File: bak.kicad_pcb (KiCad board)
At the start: 2 copper layers, 50 x 52 mm, 67 parts, among them CON1 IR_RECIEVER, CON2 HALL_SENSOR1, CON3 HALL_SENSOR2, CON4 Conn_01x03, CON5 Conn_01x03, IC1 A3G4250DTR, IC2 MCP112T-195I_TT, IC3 RN4871-V_RM140, IC4 MC3479, J1 USB_B_Micro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

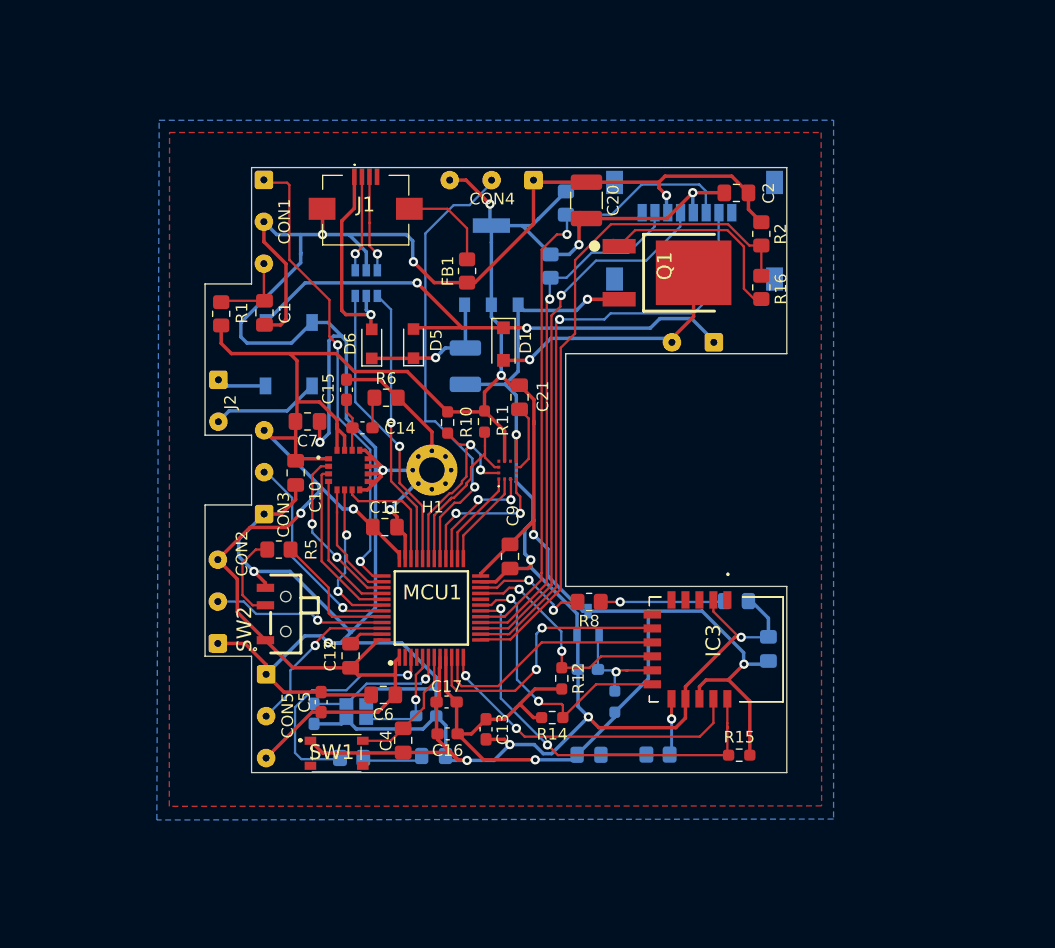
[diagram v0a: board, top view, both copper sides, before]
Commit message: update predelane piny a spi
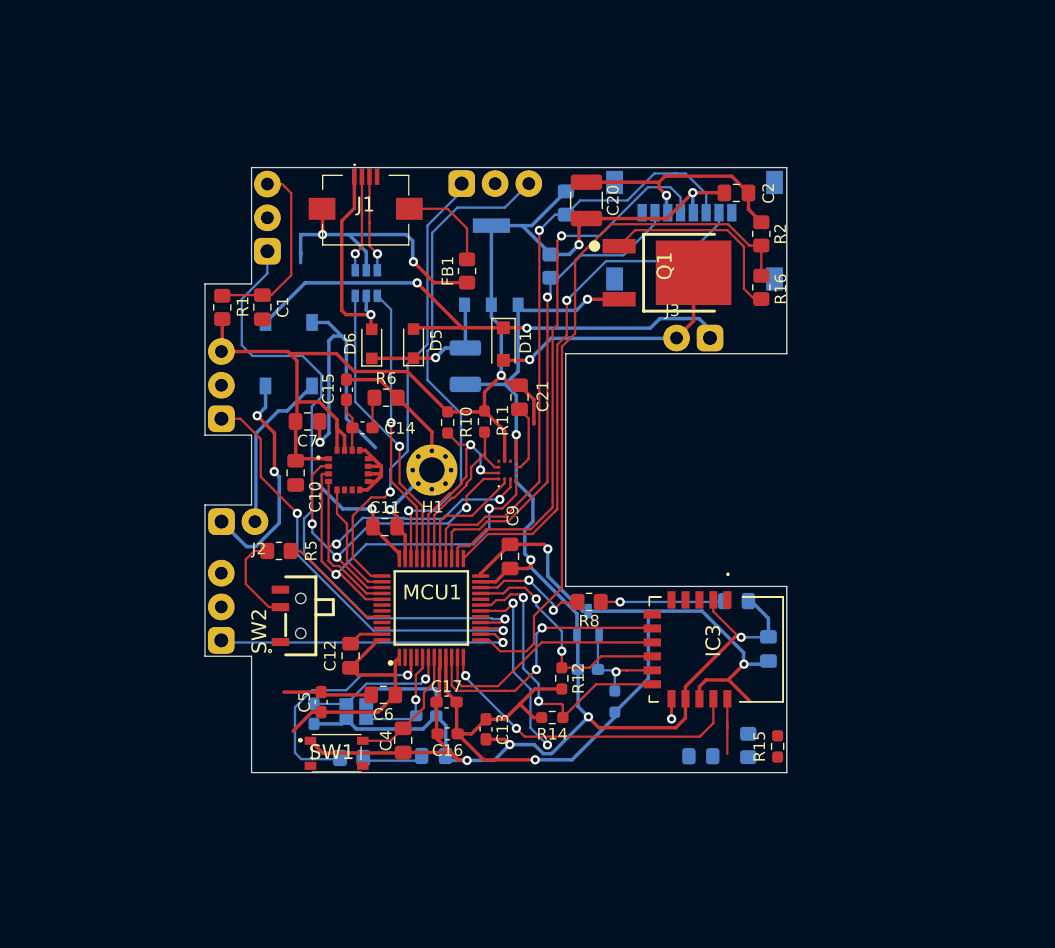
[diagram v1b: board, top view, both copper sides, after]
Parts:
- removed CON5: Conn_01x03, Connector_Wire:SolderWire-0.1sqmm_1x03_P3.6mm_D0.4mm_OD1mm
- CON1, CON2, CON3: footprint Connector_Wire:SolderWire-0.1sqmm_1x03_P3.6mm_D0.4mm_OD1mm -> KICAD_bak:MyConnector3
- CON4: value Conn_01x03 -> SWD; footprint Connector_Wire:SolderWire-0.1sqmm_1x03_P3.6mm_D0.4mm_OD1mm -> KICAD_bak:MyConnector3
- D2: value D_Bridge_+A-A -> Usměrňovací můstek ABS210-13
- IC4: value MC3479 -> Akcelerometr MC3479
- J2: footprint Connector_Wire:SolderWire-0.1sqmm_1x02_P3.6mm_D0.4mm_OD1mm -> KICAD_bak:MyConnector2
- J3: footprint Connector_Wire:SolderWire-0.1sqmm_1x02_P3.6mm_D0.4mm_OD1mm -> KICAD_bak:MyConnector2; moved to F.Cu
- moved CON3 11.7 mm to (50.1, 51.2)
- moved J2 10.3 mm to (53.0, 60.5), turned to 0 degrees
- moved D7 9.61 mm to (91.3, 83.1)
- moved R13 7.80 mm to (95.4, 82.2), turned to 270 degrees
- moved J3 3.83 mm to (89.2, 49.6)
- moved R15 3.38 mm to (97.9, 82.2), turned to 90 degrees
- moved CON4 3.31 mm to (73.7, 33.9), turned to 0 degrees
- moved CON1 3.27 mm to (54.1, 36.8), turned to 90 degrees
- moved CON2 3.15 mm to (50.1, 70.2)
- moved SW2 1.30 mm to (55.2, 70.3)
- moved R1 0.56 mm to (50.2, 44.5)
- moved C1 0.52 mm to (53.7, 44.5)
- moved R5 0.12 mm to (55.1, 65.4)
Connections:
- net /SPI3_CS renamed /SPI3_CS1
- CON2 pad 1: GND -> /HALL1
- CON2 pad 2: /HALL1 -> GND
- CON3 pad 1: GND -> /HALL2
- CON3 pad 2: /HALL2 -> GND
- CON4 pad 1: GND -> /SWCLK
- CON4 pad 2: /CON1 -> GND
- CON4 pad 3: +3.3VA -> /SWDIO
- IC4 pad 1: /SPI2_SCK -> /SPI3_SCK
- IC4 pad 2: /SPI2_CS -> /SPI3_CS2
- IC4 pad 3: /SPI2_MISO -> /SPI3_MISO
- IC4 pad 4: /SPI2_MOSI -> /SPI3_MOSI
- J4 pad 2: /SPI1_CS -> /SPI2_CS
- J4 pad 3: /SPI1_MOSI -> /SPI2_MOSI
- J4 pad 5: /SPI1_SCK -> /SPI2_SCK
- J4 pad 7: /SPI1_MISO -> /SPI2_MISO
- MCU1 pad 14: /SPI1_CS -> /HALL1
- MCU1 pad 15: /SPI1_SCK -> /HALL2
- MCU1 pad 16: /SPI1_MISO -> /IR_OUT
- MCU1 pad 17: /SPI1_MOSI -> Net-(MCU1-Pad17)
- MCU1 pad 29: /CON1 -> /SPI3_CS2
- MCU1 pad 34: /GYRO_INT -> /SWDIO
- MCU1 pad 37: /IR_OUT -> /SWCLK
- MCU1 pad 42: /GYRO_DRDY -> /I2C_SCL
- MCU1 pad 43: /HALL2 -> Net-(MCU1-Pad43)
- MCU1 pad 45: /HALL1 -> Net-(MCU1-Pad45)
- MCU1 pad 46: /CON2 -> /I2C_SDA
- R3 pad 1: /SPI1_MOSI -> /SPI2_MOSI
- R4 pad 1: /SPI1_MISO -> /SPI2_MISO
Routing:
- net GND: track 391.2 -> 271.9 mm, vias 15 -> 12
- net +3.3VA: track 293.0 -> 231.8 mm, vias 9 -> 7
- net /SPI1_MOSI: track 55.0 -> 0.00 mm, vias 1 -> 0
- net /SPI1_CS: track 52.4 -> 0.00 mm, vias 1 -> 0
- net /SPI1_SCK: track 46.5 -> 0.00 mm, vias 1 -> 0
- net /SPI1_MISO: track 45.2 -> 0.00 mm, vias 1 -> 0
- net /SWDIO: track 0.00 -> 42.8 mm, vias 0 -> 1
- net /SPI2_MOSI: track 12.8 -> 52.9 mm, vias 2 -> 1
- net /SWCLK: track 0.00 -> 39.9 mm, vias 0 -> 1
- net /SPI2_SCK: track 8.32 -> 47.8 mm, vias 0 -> 1
- net /CON1: track 39.2 -> 0.00 mm, vias 1 -> 0
- net /SPI2_CS: track 8.32 -> 45.0 mm, vias 0 -> 1
- net /SPI2_MISO: track 10.7 -> 42.0 mm, vias 2 -> 1
- net /HALL2: track 18.1 -> 39.3 mm, vias 1 -> 2
- net /SPI3_MOSI: track 14.6 -> 35.3 mm, vias 0 -> 2
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- removed copper zone on F.Cu, net (none)
- removed copper zone on B.Cu, net GND

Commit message: pred ble modulem uprava
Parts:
- added C23: 100n, Capacitor_SMD:C_0805_2012Metric_Pad1.18x1.45mm_HandSolder, F.Cu at (54.6, 76.4)
- added SW3: SW_Push_Open, SamacSys_Parts:PTS815SJM250SMTRLFS, F.Cu at (54.5, 81.0)
- U1: moved to F.Cu
- moved FB1 13.5 mm to (57.8, 41.9)
- moved U1 0.98 mm to (61.6, 42.5)
- moved SW1 0.70 mm to (60.7, 82.7)
- moved J1 0.66 mm to (62.4, 35.5), turned to 180 degrees
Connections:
- MCU1 pad 45: Net-(MCU1-Pad45) -> /BTN
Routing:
- net GND: track 271.9 -> 234.8 mm, vias 12 -> 10
- net /BTN: track 0.00 -> 16.1 mm
- net +3.3VA: track 231.8 -> 221.7 mm
- net Net-(FB1-Pad2): track 8.32 -> 0.00 mm
- net /USB_CON-: track 8.53 -> 3.13 mm, vias 1 -> 0
- net +5V: track 17.8 -> 12.7 mm, vias 1 -> 0
- net /USB_CON+: track 8.52 -> 3.65 mm, vias 1 -> 0
- net /USB+: track 24.0 -> 25.1 mm, vias 1 -> 2
- net /NRST: track 11.1 -> 10.4 mm
- net /USB-: track 25.0 -> 25.4 mm, vias 1 -> 2

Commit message: cca predelano
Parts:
- D4, D7, R13: moved to F.Cu
- R12, R15: moved to B.Cu
- moved SW3 35.0 mm to (87.8, 70.2), turned to 180 degrees
- moved C23 28.6 mm to (82.5, 70.3), turned to 90 degrees
- moved R15 14.0 mm to (84.0, 83.7), turned to 180 degrees
- moved R13 14.0 mm to (82.4, 77.2), turned to 180 degrees
- moved R12 13.5 mm to (92.3, 72.8), turned to 0 degrees
- moved R8 12.4 mm to (94.1, 69.4)
- moved D7 9.48 mm to (82.5, 79.8), turned to 0 degrees
- moved IC3 8.68 mm to (93.0, 82.6), turned to 180 degrees
- moved IC2 5.50 mm to (86.9, 73.2)
- moved D4 3.43 mm to (97.8, 70.3), turned to 90 degrees
- moved C19 2.82 mm to (81.0, 78.4), turned to 270 degrees
- moved R5 1.50 mm to (53.6, 65.5)
- moved R14 1.49 mm to (79.0, 78.3), turned to 270 degrees
- moved C22 1.06 mm to (96.2, 73.3)
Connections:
- MCU1 pad 17: Net-(MCU1-Pad17) -> /BTN
- MCU1 pad 45: /BTN -> Net-(MCU1-Pad45)
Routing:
- net GND: track 234.8 -> 302.5 mm, vias 10 -> 15
- net +3.3VA: track 221.7 -> 272.2 mm, vias 7 -> 11
- net /DIODE2: track 10.3 -> 24.0 mm
- net /UART_RX: track 20.7 -> 30.2 mm
- net /UART_TX: track 23.9 -> 32.8 mm
- net Net-(D4-Pad2): track 10.7 -> 2.71 mm, vias 1 -> 0
- net /MODE: track 21.4 -> 28.0 mm
- net /UART_RTS: track 20.4 -> 26.1 mm
- net Net-(FB1-Pad2): track 0.00 -> 5.62 mm
- net /UART_TX_IND: track 27.8 -> 22.3 mm, vias 2 -> 4
- net /RST: track 9.17 -> 14.0 mm
- net /P0_2: track 1.73 -> 6.04 mm, vias 1 -> 0
- net Net-(D7-Pad1): track 0.00 -> 2.62 mm
- net /BTN: track 16.1 -> 13.8 mm, vias 0 -> 2
- net /UART_CTS: track 25.8 -> 27.7 mm
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- added copper zone on B.Cu, net GND
- added copper zone on F.Cu, net GND

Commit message: hotovo_snad
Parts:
- C2, C20, Q1, R16, R2: moved to B.Cu
- J4: moved to F.Cu
- moved R16 12.2 mm to (85.0, 46.8), turned to 180 degrees
- moved R2 10.5 mm to (91.2, 47.3), turned to 180 degrees
- moved C20 10.2 mm to (91.7, 35.1), turned to 180 degrees
- moved J3 7.85 mm to (94.9, 44.1), turned to 90 degrees
- moved J4 4.16 mm to (86.7, 39.4), turned to 180 degrees
- moved C2 2.72 mm to (97.1, 34.6), turned to 90 degrees
- moved FB1 2.43 mm to (57.7, 44.3)
- moved Q1 1.36 mm to (91.8, 40.8), turned to 90 degrees
- moved D3 0.99 mm to (67.8, 82.2)
- moved R7 0.89 mm to (61.2, 82.3)
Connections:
- net /I2C_SDA renamed Net-(MCU1-Pad46)
- MCU1 pad 38: /SPI3_CS1 -> /GYRO_INT
- MCU1 pad 42: /I2C_SCL -> /GYRO_DRDY
- MCU1 pad 43: Net-(MCU1-Pad43) -> /SPI3_CS1
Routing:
- net GND: track 302.5 -> 342.4 mm, vias 15 -> 17
- net +3.3VA: track 272.2 -> 306.3 mm, vias 11 -> 13
- net /GYRO_DRDY: track 0.00 -> 16.4 mm, vias 0 -> 2
- net /MOTOR_PWM: track 61.6 -> 46.4 mm, vias 0 -> 1
- net Net-(Q1-Pad1): track 19.1 -> 4.57 mm
- net /MOTOR-: track 21.3 -> 33.9 mm, vias 1 -> 3
- net /GYRO_INT: track 0.00 -> 9.66 mm
- net /SPI2_MOSI: track 52.9 -> 44.5 mm, vias 1 -> 2
- net /SPI2_CS: track 43.7 -> 36.3 mm, vias 1 -> 0
- net /SPI3_CS1: track 10.2 -> 16.6 mm, vias 0 -> 2
- net /MOTOR+: track 47.8 -> 51.7 mm, vias 2 -> 3
- net /SPI2_MISO: track 42.0 -> 46.0 mm, vias 1 -> 2
- net Net-(FB1-Pad2): track 5.62 -> 8.10 mm
- net /IR_OUT: track 55.2 -> 56.9 mm
- net /SPI2_SCK: track 47.0 -> 45.5 mm, vias 1 -> 0
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- removed copper zone on B.Cu, net GND
- removed copper zone on F.Cu, net GND

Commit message: snad final, zony, upraveny 3D modely, upraveny tlacitko
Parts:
- removed C23: 100n, Capacitor_SMD:C_0805_2012Metric_Pad1.18x1.45mm_HandSolder
- added R17: 10k, Resistor_SMD:R_0805_2012Metric_Pad1.20x1.40mm_HandSolder, F.Cu at (81.6, 70.4)
- moved C6 0.15 mm to (63.9, 77.7)
- moved Q1 0.08 mm to (91.8, 40.7)
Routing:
- net GND: track 342.4 -> 363.6 mm, vias 17 -> 19
- net +3.3VA: track 306.3 -> 308.9 mm, vias 13 -> 14
- net /BTN: track 13.8 -> 15.7 mm
- added copper zone on B.Cu, net GND
- added copper zone on F.Cu, net GND

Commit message: final_version2_snad
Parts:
- removed FB1: Ferrite_Bead, Resistor_SMD:R_0805_2012Metric_Pad1.20x1.40mm_HandSolder
- added R18: 22, Resistor_SMD:R_0603_1608Metric_Pad0.98x0.95mm_HandSolder, B.Cu at (66.6, 44.7)
- added R19: 22, Resistor_SMD:R_0603_1608Metric_Pad0.98x0.95mm_HandSolder, F.Cu at (60.2, 46.3)
- J2: value Conn_01x02 -> Conn_01x02_MountingPin; footprint KICAD_bak:MyConnector2 -> KICAD_bak:Conn01x02_my
- moved CON2 10.7 mm to (54.0, 80.2)
- moved R5 7.99 mm to (49.9, 72.6), turned to 90 degrees
- moved J2 5.29 mm to (52.6, 65.8), turned to 90 degrees
- moved J1 0.34 mm to (62.0, 35.4)
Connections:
- J1 pad 6: Net-(FB1-Pad2) -> GND
- U1 pad 4: /USB+ -> Net-(R19-Pad1)
- U1 pad 6: /USB- -> Net-(R18-Pad2)
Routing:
- net Net-(FB1-Pad2): track 8.10 -> 0.00 mm
- net Net-(D2-Pad4): track 14.2 -> 19.0 mm, vias 0 -> 1
- net GND: track 363.6 -> 368.3 mm, vias 19 -> 20
- net Net-(R18-Pad2): track 0.00 -> 3.86 mm, vias 0 -> 1
- net /USB-: track 25.4 -> 21.8 mm, vias 2 -> 1
- net /BOOT: track 11.8 -> 15.3 mm
- net /USB+: track 25.1 -> 22.2 mm
- net /HALL1: track 27.4 -> 29.8 mm
- net +3.3VA: track 308.9 -> 306.6 mm, vias 14 -> 15
- net Net-(R19-Pad1): track 0.00 -> 1.67 mm
- net /SPI3_MOSI: track 35.1 -> 35.6 mm
- net Net-(R5-Pad2): track 6.45 -> 5.88 mm
- net Net-(D2-Pad2): vias 2 -> 3
